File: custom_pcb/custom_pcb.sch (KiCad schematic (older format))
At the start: 303 parts, among them J1 USB_mini_micro_B, K0 KEYSW, K1 KEYSW, K10 KEYSW, K11 KEYSW, K12 KEYSW, K13 KEYSW, K14 KEYSW, K15 KEYSW, K16 KEYSW, K17 KEYSW, K18 KEYSW, K19 KEYSW, K2 KEYSW, K20 KEYSW, K21 KEYSW, K22 KEYSW, K23 KEYSW, K24 KEYSW, K25 KEYSW, K26 KEYSW, K27 KEYSW, K28 KEYSW, K29 KEYSW, K3 KEYSW, K30 KEYSW, K31 KEYSW, K32 KEYSW, K33 KEYSW, K34 KEYSW, K35 KEYSW, K36 KEYSW, K37 KEYSW, K38 KEYSW, K39 KEYSW, K4 KEYSW, K40 KEYSW, K41 KEYSW, K42 KEYSW, K43 KEYSW, K44 KEYSW, K45 KEYSW, K46 KEYSW, K47 KEYSW, K48 KEYSW, K49 KEYSW, K5 KEYSW, K50 KEYSW, K51 KEYSW, K52 KEYSW, K53 KEYSW, K54 KEYSW, K55 KEYSW, K56 KEYSW, K57 KEYSW, K58 KEYSW, K59 KEYSW, K6 KEYSW, K63 KEYSW, K64 KEYSW, K65 KEYSW, K66 KEYSW, K67 KEYSW, K68 KEYSW, K69 KEYSW, K7 KEYSW, K70 KEYSW, K71 KEYSW, K72 KEYSW, K73 KEYSW, K74 KEYSW, K75 KEYSW, K76 KEYSW, K77 KEYSW, K78 KEYSW, K79 KEYSW, K8 KEYSW, K80 KEYSW, K81 KEYSW, K82 KEYSW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

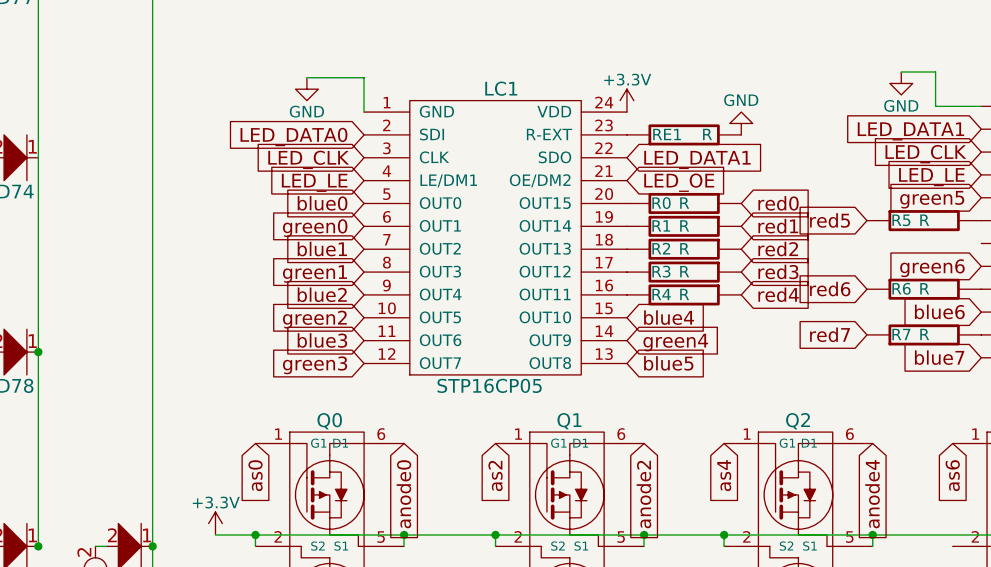
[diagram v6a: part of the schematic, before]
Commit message: module for MKL04 and more routing
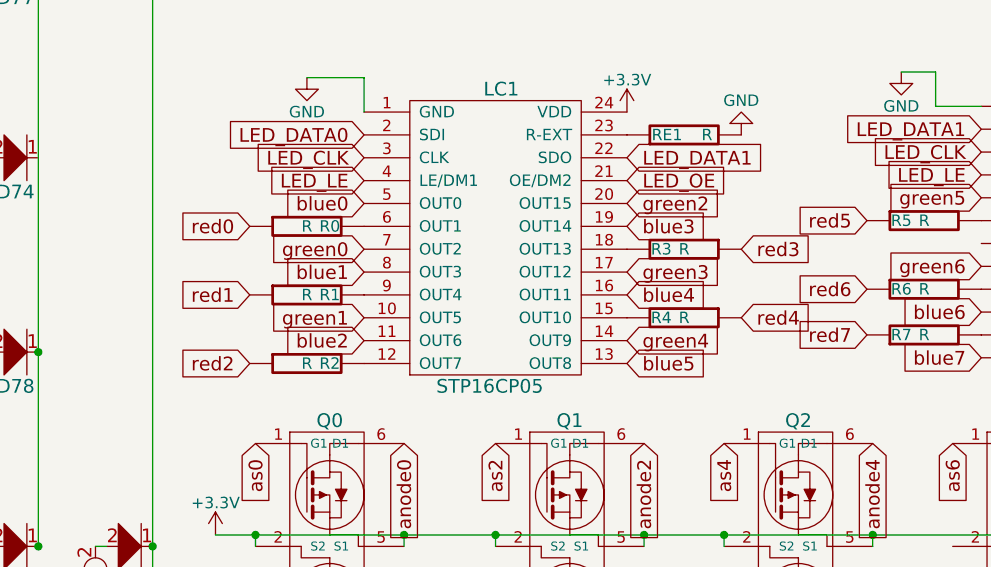
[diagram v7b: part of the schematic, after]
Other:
- moved on the sheet: R0, R1, R2, R3, R4
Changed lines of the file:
@@
 L R R4
 U 1 1 58B80FEF
-P 10275 8750
-F 0 "R4" V 10275 8650 50  0000 C CNN
-F 1 "R" V 10275 8750 50  0000 C CNN
-F 2 "Resistors_SMD:R_0402_NoSilk" H 10275 8750 60  0001 C CNN
-F 3 "" H 10275 8750 60  0000 C CNN
-	1    10275 8750
+P 10275 8850
+F 0 "R4" V 10275 8750 50  0000 C CNN
+F 1 "R" V 10275 8850 50  0000 C CNN
+F 2 "Resistors_SMD:R_0402_NoSilk" H 10275 8850 60  0001 C CNN
+F 3 "" H 10275 8850 60  0000 C CNN
+	1    10275 8850
 	0    1    1    0
 $EndComp
@@
 L R R3
 U 1 1 58B80FF6
-P 10275 8650
-F 0 "R3" V 10275 8550 50  0000 C CNN
-F 1 "R" V 10275 8650 50  0000 C CNN
-F 2 "Resistors_SMD:R_0402_NoSilk" H 10275 8650 60  0001 C CNN
-F 3 "" H 10275 8650 60  0000 C CNN
-	1    10275 8650
+P 10275 8550
+F 0 "R3" V 10275 8450 50  0000 C CNN
+F 1 "R" V 10275 8550 50  0000 C CNN
+F 2 "Resistors_SMD:R_0402_NoSilk" H 10275 8550 60  0001 C CNN
+F 3 "" H 10275 8550 60  0000 C CNN
+	1    10275 8550
 	0    1    1    0
 $EndComp
@@
 L R R2
 U 1 1 58B81E39
-P 10275 8550
-F 0 "R2" V 10275 8450 50  0000 C CNN
-F 1 "R" V 10275 8550 50  0000 C CNN
-F 2 "Resistors_SMD:R_0402_NoSilk" H 10275 8550 60  0001 C CNN
-F 3 "" H 10275 8550 60  0000 C CNN
-	1    10275 8550
-	0    1    1    0
+P 8625 9050
+F 0 "R2" V 8625 8950 50  0000 C CNN
+F 1 "R" V 8625 9050 50  0000 C CNN
+F 2 "Resistors_SMD:R_0402_NoSilk" H 8625 9050 60  0001 C CNN
+F 3 "" H 8625 9050 60  0000 C CNN
+	1    8625 9050
+	0    -1   1    0
 $EndComp
 Text GLabel 10350 950  0    60   Input ~ 0
@@
 L R R1
 U 1 1 58B81E40
-P 10275 8450
-F 0 "R1" V 10275 8350 50  0000 C CNN
-F 1 "R" V 10275 8450 50  0000 C CNN
-F 2 "Resistors_SMD:R_0402_NoSilk" H 10275 8450 60  0001 C CNN
-F 3 "" H 10275 8450 60  0000 C CNN
-	1    10275 8450
-	0    1    1    0
+P 8625 8750
+F 0 "R1" V 8625 8650 50  0000 C CNN
+F 1 "R" V 8625 8750 50  0000 C CNN
+F 2 "Resistors_SMD:R_0402_NoSilk" H 8625 8750 60  0001 C CNN
+F 3 "" H 8625 8750 60  0000 C CNN
+	1    8625 8750
+	0    -1   1    0
 $EndComp
 Text GLabel 9850 950  0    60   Input ~ 0
@@
 L R R0
 U 1 1 58B827F9
-P 10275 8350
-F 0 "R0" V 10275 8250 50  0000 C CNN
-F 1 "R" V 10275 8350 50  0000 C CNN
-F 2 "Resistors_SMD:R_0402_NoSilk" H 10275 8350 60  0001 C CNN
-F 3 "" H 10275 8350 60  0000 C CNN
-	1    10275 8350
-	0    1    1    0
+P 8625 8450
+F 0 "R0" V 8625 8350 50  0000 C CNN
+F 1 "R" V 8625 8450 50  0000 C CNN
+F 2 "Resistors_SMD:R_0402_NoSilk" H 8625 8450 60  0001 C CNN
+F 3 "" H 8625 8450 60  0000 C CNN
+	1    8625 8450
+	0    -1   1    0
 $EndComp
 Text GLabel 15950 1400 2    60   Input ~ 0
@@
 Text GLabel 8875 8350 0    60   Input ~ 0
 blue0
-Text GLabel 8875 8450 0    60   Input ~ 0
+Text GLabel 8875 8550 0    60   Input ~ 0
 green0
-Text GLabel 8875 8550 0    60   Input ~ 0
+Text GLabel 8875 8650 0    60   Input ~ 0
 blue1
-Text GLabel 8875 8650 0    60   Input ~ 0
+Text GLabel 8875 8850 0    60   Input ~ 0
 green1
-Text GLabel 8875 8750 0    60   Input ~ 0
+Text GLabel 8875 8950 0    60   Input ~ 0
 blue2
-Text GLabel 8875 8850 0    60   Input ~ 0
+Text GLabel 10025 8350 2    60   Input ~ 0
 green2
-Text GLabel 8875 8950 0    60   Input ~ 0
+Text GLabel 10025 8450 2    60   Input ~ 0
 blue3
-Text GLabel 8875 9050 0    60   Input ~ 0
+Text GLabel 10025 8650 2    60   Input ~ 0
 green3
-Text GLabel 10025 8850 2    60   Input ~ 0
+Text GLabel 10025 8750 2    60   Input ~ 0
 blue4
 Text GLabel 10025 8950 2    60   Input ~ 0
@@
 Text GLabel 11075 8425 0    60   Input ~ 0
 red5
-Text GLabel 10525 8750 2    60   Input ~ 0
+Text GLabel 10525 8850 2    60   Input ~ 0
 red4
-Text GLabel 10525 8650 2    60   Input ~ 0
+Text GLabel 10525 8550 2    60   Input ~ 0
 red3
-Text GLabel 10525 8550 2    60   Input ~ 0
+Text GLabel 8375 9050 0    60   Input ~ 0
 red2
-Text GLabel 10525 8450 2    60   Input ~ 0
+Text GLabel 8375 8750 0    60   Input ~ 0
 red1
-Text GLabel 10525 8350 2    60   Input ~ 0
+Text GLabel 8375 8450 0    60   Input ~ 0
 red0
 Text GLabel 7875 2750 0    60   Input ~ 0

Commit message: small fixes and checkpoint for moving the leds
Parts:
- added D60: D, Diodes_SMD:D_SOD-123, symbol D
- added K60: KEYSW, cherry_rgb:CHERRY_PLATE_100H, symbol KEYSW
- K10, K11, K12, K13, K14, K15, K16, K17, K18, K19, K21, K22, K23, K24, K25, K26, K27, K28, K29, K31, K32, K33, K34, K35, K36, K37, K38, K39, K41, K42, K43, K44, K45, K46, K47, K48, K49, K50, K52, K53, K57, K58, K59, K65, K66, K69, K70, K71, K72, K73, K75, K76, K77, K79, K80, K82, K84, K85, K86, MOUSE1: footprint cherry_rgb:CHERRY_PLATE_NH_100H -> cherry_rgb:CHERRY_PLATE_100H
- K83: footprint cherry_rgb:CHERRY_PLATE_275H -> cherry_rgb:CHERRY_PLATE_175_275H
- R0, R1, R10, R11, R12, R13, R14, R15, R2, R3, R4, R5, R6, R7, R8, R9: footprint Resistors_SMD:R_0402_NoSilk -> Resistors_SMD:R_0603_HandSoldering
- RE0, RE1, RE2: footprint Resistors_SMD:R_0402 -> Resistors_SMD:R_0603_HandSoldering
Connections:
- wire segments 2539 -> 2540
